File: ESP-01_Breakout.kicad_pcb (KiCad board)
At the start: 2 copper layers, 88.9 x 25.4 mm, 136 parts, among them J1 TBL003-254-02GR-2OR, SW1 SW_SPDT, U1 ESP-01v090, U2 R-78E5.0-0.5, U3 R-78E3.3-0.5

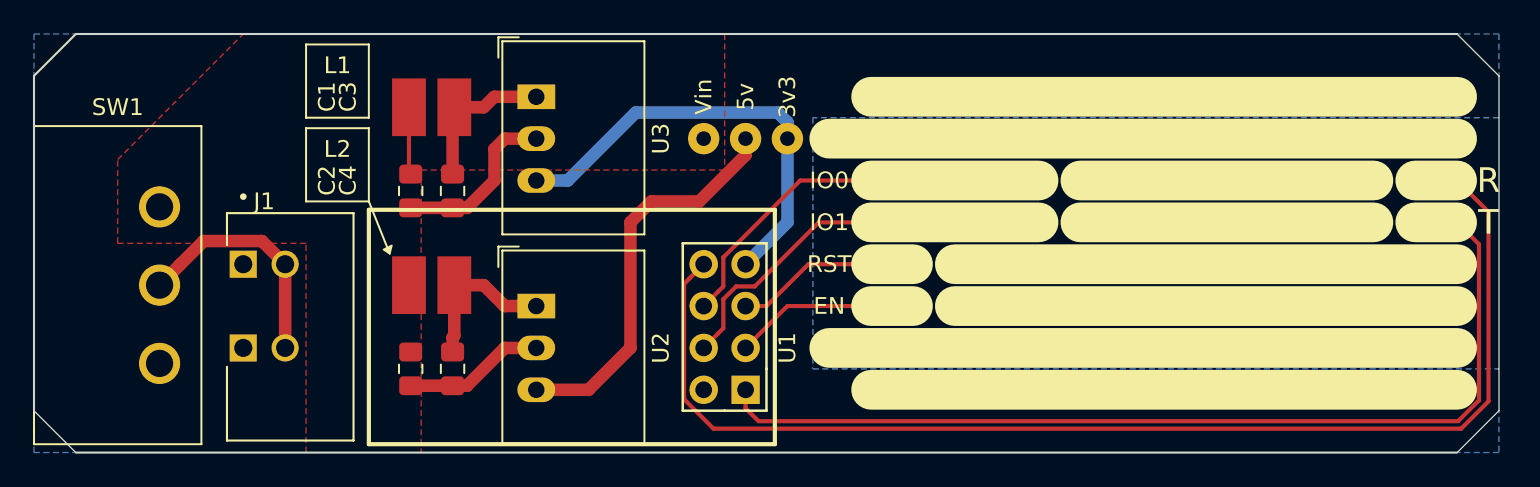
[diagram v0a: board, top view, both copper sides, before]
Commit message: Barrel Jack, Smaller Switch
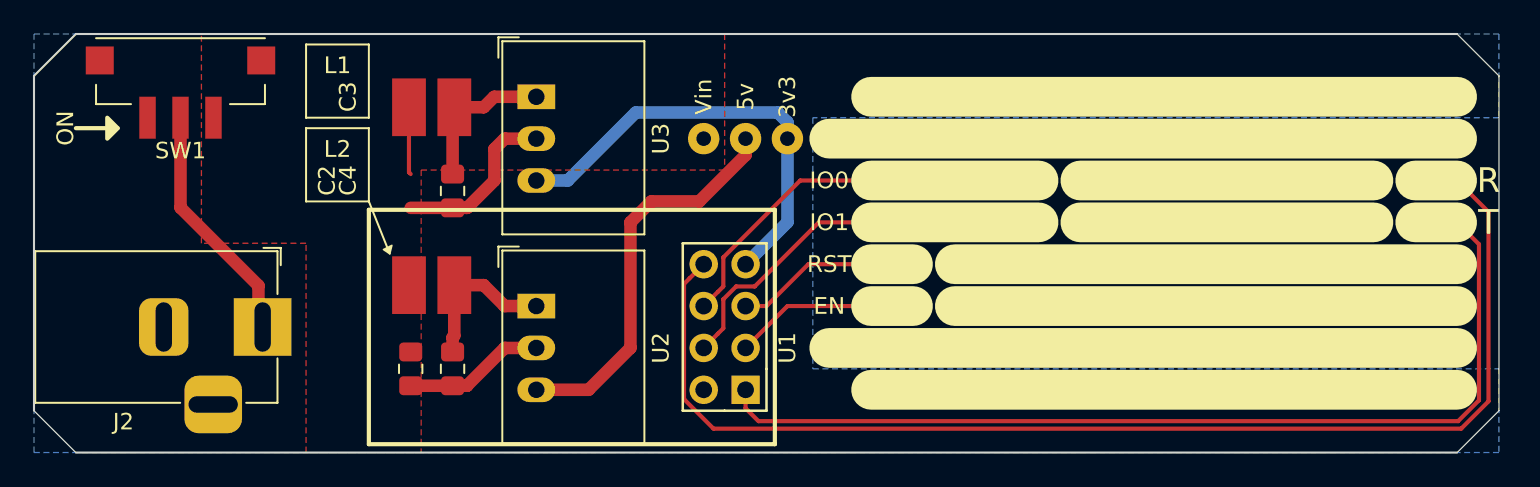
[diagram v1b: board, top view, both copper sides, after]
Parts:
- removed C1: 4.7uF, Capacitor_SMD:C_0805_2012Metric_Pad1.15x1.40mm_HandSolder
- removed J1: TBL003-254-02GR-2OR, TBL003-254-02GR-2OR:CUI_TBL003-254-02GR-2OR
- added J2: Barrel_Jack_Switch, ESP-01_Breakout:BarrelJack_Horizontal, F.Cu at (133.3, 95.2)
- added REF**: Symbol_Barrel_Polarity, Symbol:Symbol_Barrel_Polarity, B.Cu at (123.2, 95.3)
- SW1: footprint ESP-01_Breakout:L102011ML04Q -> ESP-01_Breakout:SS312SAH4-R
- moved SW1 10.2 mm to (128.3, 82.5)
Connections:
- SW1 pad 1: +12V -> /Off
- SW1 pad 3: /Off -> +12V
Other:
- board text added: "+"
- board text added: "-"
- board text added: "6-28v"
- board text added: "ON"
- board text removed: "- +"
- board text removed: "Vin: 6-28v"

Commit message: BOM, gitignore Update
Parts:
- added C1: 4.7uF, Capacitor_SMD:C_0805_2012Metric_Pad1.15x1.40mm_HandSolder, F.Cu at (142.2, 87.0)
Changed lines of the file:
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@@
     (tracks 87)
     (zones 0)
-    (modules 136)
+    (modules 137)
     (nets 22)
   )
   (page A4)
   (layers
-    (0 F.Cu signal hide)
-    (31 B.Cu signal)
+    (0 F.Cu signal)
+    (31 B.Cu signal hide)
     (32 B.Adhes user hide)
     (33 F.Adhes user hide)
-    (34 B.Paste user)
-    (35 F.Paste user hide)
-    (36 B.SilkS user)
-    (37 F.SilkS user hide)
-    (38 B.Mask user)
-    (39 F.Mask user hide)
+    (34 B.Paste user hide)
+    (35 F.Paste user)
+    (36 B.SilkS user hide)
+    (37 F.SilkS user)
+    (38 B.Mask user hide)
+    (39 F.Mask user)
     (40 Dwgs.User user hide)
     (41 Cmts.User user hide)
@@
     (44 Edge.Cuts user)
     (45 Margin user hide)
-    (46 B.CrtYd user)
-    (47 F.CrtYd user hide)
-    (48 B.Fab user)
-    (49 F.Fab user hide)
+    (46 B.CrtYd user hide)
+    (47 F.CrtYd user)
+    (48 B.Fab user hide)
+    (49 F.Fab user)
   )
   (setup
@@
       (usegerberattributes false)
       (usegerberadvancedattributes false)
-      (creategerberjobfile true)
+      (creategerberjobfile false)
       (excludeedgelayer true)
       (linewidth 0.127000)
@@
     (add_net "Net-(J2-Pad3)")
   )
+  (module Capacitor_SMD:C_0805_2012Metric_Pad1.15x1.40mm_HandSolder (layer F.Cu)
+    (at 142.24 86.995 270)
+    (descr "Capacitor SMD 0805 (2012 Metric), square (rectangular) end terminal, IPC_7351 nominal with elongated pad for handsoldering. (Body size source: https://docs.google.com/spreadsheets/d/1BsfQQcO9C6DZCsRaXUlFlo91Tg2WpOkGARC1WS5S8t0/edit?usp=sharing), generated with kicad-footprint-generator")
+    (tags "capacitor handsolder")
+    (attr smd)
+    (fp_text reference C1 (at -5.715 5.08 90) (layer F.SilkS)
+      (effects (font (size 1 1) (thickness 0.15)))
+    )
+    (fp_text value 4.7uF (at 0 1.65 90) (layer F.Fab)
+      (effects (font (size 1 1) (thickness 0.15)))
+    )
+    (fp_line (start 1.85 0.95) (end -1.85 0.95) (layer F.CrtYd) (width 0.05))
+    (fp_line (start 1.85 -0.95) (end 1.85 0.95) (layer F.CrtYd) (width 0.05))
+    (fp_line (start -1.85 -0.95) (end 1.85 -0.95) (layer F.CrtYd) (width 0.05))
+    (fp_line (start -1.85 0.95) (end -1.85 -0.95) (layer F.CrtYd) (width 0.05))
+    (fp_line (start -0.261252 0.71) (end 0.261252 0.71) (layer F.SilkS) (width 0.12))
+    (fp_line (start -0.261252 -0.71) (end 0.261252 -0.71) (layer F.SilkS) (width 0.12))
+    (fp_line (start 1 0.6) (end -1 0.6) (layer F.Fab) (width 0.1))
+    (fp_line (start 1 -0.6) (end 1 0.6) (layer F.Fab) (width 0.1))
+    (fp_line (start -1 -0.6) (end 1 -0.6) (layer F.Fab) (width 0.1))
+    (fp_line (start -1 0.6) (end -1 -0.6) (layer F.Fab) (width 0.1))
+    (pad 2 smd roundrect (at 1.025 0 270) (size 1.15 1.4) (layers F.Cu F.Paste F.Mask) (roundrect_rratio 0.217391)
+      (net 1 GND))
+    (pad 1 smd roundrect (at -1.025 0 270) (size 1.15 1.4) (layers F.Cu F.Paste F.Mask) (roundrect_rratio 0.217391)
+      (net 2 +12V))
+    (model ${KISYS3DMOD}/Capacitor_SMD.3dshapes/C_0805_2012Metric.wrl
+      (at (xyz 0 0 0))
+      (scale (xyz 1 1 1))
+      (rotate (xyz 0 0 0))
+    )
+  )
   (module Symbol:Symbol_Barrel_Polarity (layer B.Cu)

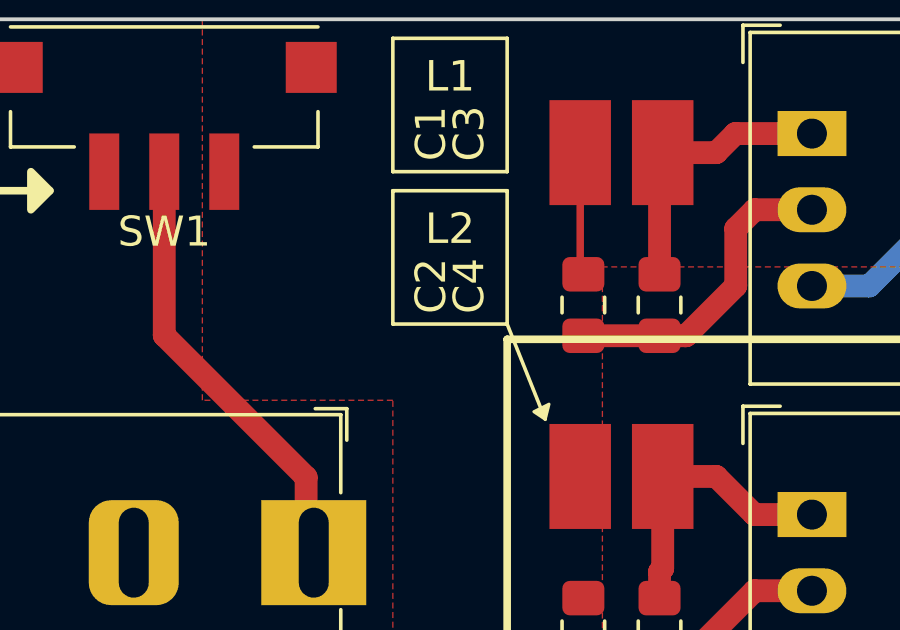
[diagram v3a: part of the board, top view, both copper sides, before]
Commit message: Add Inductor 3D Model
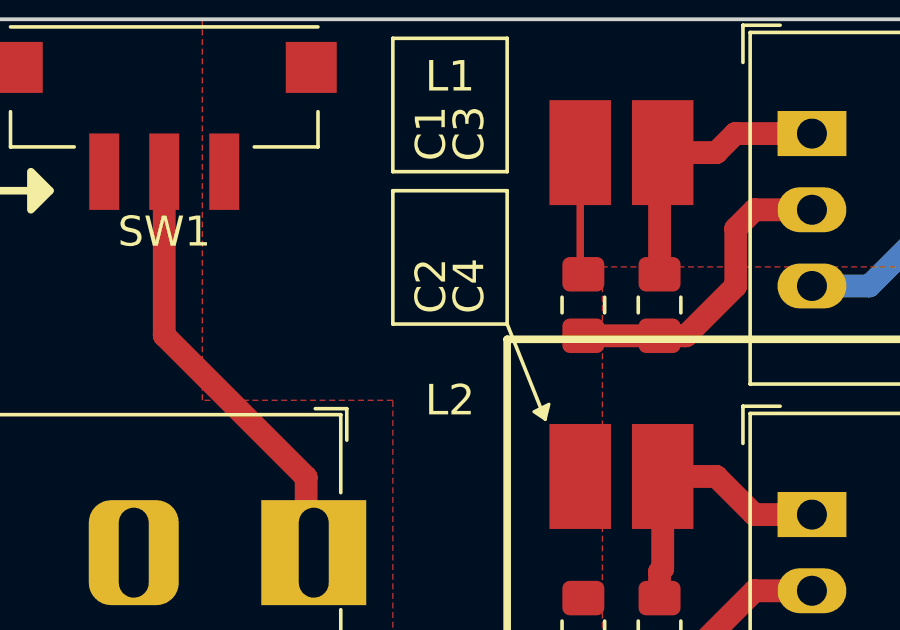
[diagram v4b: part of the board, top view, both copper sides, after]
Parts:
- L1, L2: footprint RLS-397:IND_RLS-397 -> ESP-01_Breakout:IND_RLS-397
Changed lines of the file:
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@@
     (solder_mask_min_width 0.25)
     (aux_axis_origin 0 0)
+    (grid_origin 119.38 102.87)
     (visible_elements FFFDFF7F)
     (pcbplotparams
@@
     (add_net "Net-(J2-Pad3)")
   )
+  (module ESP-01_Breakout:IND_RLS-397 (layer F.Cu)
+    (at 143.51 92.71)
+    (fp_text reference L2 (at -5.715 -2.54 180) (layer F.SilkS)
+      (effects (font (size 1.016 1.016) (thickness 0.1524)))
+    )
+    (fp_text value L (at 2.788 2.792) (layer F.Fab)
+      (effects (font (size 0.8 0.8) (thickness 0.015)))
+    )
+    (fp_line (start -2.25 -1.6) (end 2.25 -1.6) (layer F.Fab) (width 0.127))
+    (fp_line (start 2.25 -1.6) (end 2.25 1.6) (layer F.Fab) (width 0.127))
+    (fp_line (start 2.25 1.6) (end -2.25 1.6) (layer F.Fab) (width 0.127))
+    (fp_line (start -2.25 1.6) (end -2.25 -1.6) (layer F.Fab) (width 0.127))
+    (fp_line (start -2.66 -2.01) (end 2.66 -2.01) (layer F.CrtYd) (width 0.05))
+    (fp_line (start 2.66 -2.01) (end 2.66 2.01) (layer F.CrtYd) (width 0.05))
+    (fp_line (start 2.66 2.01) (end -2.66 2.01) (layer F.CrtYd) (width 0.05))
+    (fp_line (start -2.66 2.01) (end -2.66 -2.01) (layer F.CrtYd) (width 0.05))
+    (pad 1 smd rect (at -1.375 0) (size 2.05 3.5) (layers F.Cu F.Paste F.Mask)
+      (net 2 +12V))
+    (pad 2 smd rect (at 1.375 0) (size 2.05 3.5) (layers F.Cu F.Paste F.Mask)
+      (net 4 "Net-(C4-Pad1)"))
+    (model ${KIPRJMOD}/3D_Files/RLS-126-R--3DModel-STEP-1.STEP
+      (at (xyz 0 0 0))
+      (scale (xyz 1 1 1))
+      (rotate (xyz -90 0 0))
+    )
+  )
+  (module ESP-01_Breakout:IND_RLS-397 (layer F.Cu)
+    (at 143.51 81.915)
+    (fp_text reference L1 (at -5.715 -2.54 180) (layer F.SilkS)
+      (effects (font (size 1.016 1.016) (thickness 0.1524)))
+    )
+    (fp_text value L (at 2.788 2.792) (layer F.Fab)
+      (effects (font (size 0.8 0.8) (thickness 0.015)))
+    )
+    (fp_line (start -2.25 -1.6) (end 2.25 -1.6) (layer F.Fab) (width 0.127))
+    (fp_line (start 2.25 -1.6) (end 2.25 1.6) (layer F.Fab) (width 0.127))
+    (fp_line (start 2.25 1.6) (end -2.25 1.6) (layer F.Fab) (width 0.127))
+    (fp_line (start -2.25 1.6) (end -2.25 -1.6) (layer F.Fab) (width 0.127))
+    (fp_line (start -2.66 -2.01) (end 2.66 -2.01) (layer F.CrtYd) (width 0.05))
+    (fp_line (start 2.66 -2.01) (end 2.66 2.01) (layer F.CrtYd) (width 0.05))
+    (fp_line (start 2.66 2.01) (end -2.66 2.01) (layer F.CrtYd) (width 0.05))
+    (fp_line (start -2.66 2.01) (end -2.66 -2.01) (layer F.CrtYd) (width 0.05))
+    (pad 1 smd rect (at -1.375 0) (size 2.05 3.5) (layers F.Cu F.Paste F.Mask)
+      (net 2 +12V))
+    (pad 2 smd rect (at 1.375 0) (size 2.05 3.5) (layers F.Cu F.Paste F.Mask)
+      (net 3 "Net-(C3-Pad1)"))
+    (model ${KIPRJMOD}/3D_Files/RLS-126-R--3DModel-STEP-1.STEP
+      (at (xyz 0 0 0))
+      (scale (xyz 1 1 1))
+      (rotate (xyz -90 0 0))
+    )
+  )
   (module ESP-01_Breakout:SS312SAH4-R (layer F.Cu)
     (at 128.27 82.55 270)
@@
     (fp_text value 4.7uF (at 0 1.65 90) (layer F.Fab)
       (effects (font (size 1 1) (thickness 0.15)))
+    )
+    (fp_text user %R (at 0 0 90) (layer F.Fab)
+      (effects (font (size 0.5 0.5) (thickness 0.08)))
     )
     (fp_line (start 1.85 0.95) (end -1.85 0.95) (layer F.CrtYd) (width 0.05))
@@
       (rotate (xyz -90 0 90))
     )
-  )
-  (module RLS-397:IND_RLS-397 (layer F.Cu)
-    (at 143.51 81.915)
-    (fp_text reference L1 (at -5.715 -2.54 180) (layer F.SilkS)
-      (effects (font (size 1.016 1.016) (thickness 0.1524)))
-    )
-    (fp_text value L (at 2.788 2.792) (layer F.Fab)
-      (effects (font (size 0.8 0.8) (thickness 0.015)))
-    )
-    (fp_line (start -2.66 2.01) (end -2.66 -2.01) (layer F.CrtYd) (width 0.05))
-    (fp_line (start 2.66 2.01) (end -2.66 2.01) (layer F.CrtYd) (width 0.05))
-    (fp_line (start 2.66 -2.01) (end 2.66 2.01) (layer F.CrtYd) (width 0.05))
-    (fp_line (start -2.66 -2.01) (end 2.66 -2.01) (layer F.CrtYd) (width 0.05))
-    (fp_line (start -2.25 1.6) (end -2.25 -1.6) (layer F.Fab) (width 0.127))
-    (fp_line (start 2.25 1.6) (end -2.25 1.6) (layer F.Fab) (width 0.127))
-    (fp_line (start 2.25 -1.6) (end 2.25 1.6) (layer F.Fab) (width 0.127))
-    (fp_line (start -2.25 -1.6) (end 2.25 -1.6) (layer F.Fab) (width 0.127))
-    (pad 2 smd rect (at 1.375 0) (size 2.05 3.5) (layers F.Cu F.Paste F.Mask)
-      (net 3 "Net-(C3-Pad1)"))
-    (pad 1 smd rect (at -1.375 0) (size 2.05 3.5) (layers F.Cu F.Paste F.Mask)
-      (net 2 +12V))
   )
   (module ESP-01_Breakout:TP (layer F.Cu)
@@
     )
   )
-  (module RLS-397:IND_RLS-397 (layer F.Cu)
-    (at 143.51 92.71)
-    (fp_text reference L2 (at -5.715 -8.255) (layer F.SilkS)
-      (effects (font (size 1.016 1.016) (thickness 0.1524)))
-    )
-    (fp_text value L (at 2.788 2.792) (layer F.Fab)
-      (effects (font (size 0.8 0.8) (thickness 0.015)))
-    )
-    (fp_line (start -2.66 2.01) (end -2.66 -2.01) (layer F.CrtYd) (width 0.05))
-    (fp_line (start 2.66 2.01) (end -2.66 2.01) (layer F.CrtYd) (width 0.05))
-    (fp_line (start 2.66 -2.01) (end 2.66 2.01) (layer F.CrtYd) (width 0.05))
-    (fp_line (start -2.66 -2.01) (end 2.66 -2.01) (layer F.CrtYd) (width 0.05))
-    (fp_line (start -2.25 1.6) (end -2.25 -1.6) (layer F.Fab) (width 0.127))
-    (fp_line (start 2.25 1.6) (end -2.25 1.6) (layer F.Fab) (width 0.127))
-    (fp_line (start 2.25 -1.6) (end 2.25 1.6) (layer F.Fab) (width 0.127))
-    (fp_line (start -2.25 -1.6) (end 2.25 -1.6) (layer F.Fab) (width 0.127))
-    (pad 2 smd rect (at 1.375 0) (size 2.05 3.5) (layers F.Cu F.Paste F.Mask)
-      (net 4 "Net-(C4-Pad1)"))
-    (pad 1 smd rect (at -1.375 0) (size 2.05 3.5) (layers F.Cu F.Paste F.Mask)
-      (net 2 +12V))
-  )
   (module Capacitor_SMD:C_0805_2012Metric_Pad1.15x1.40mm_HandSolder (layer F.Cu)

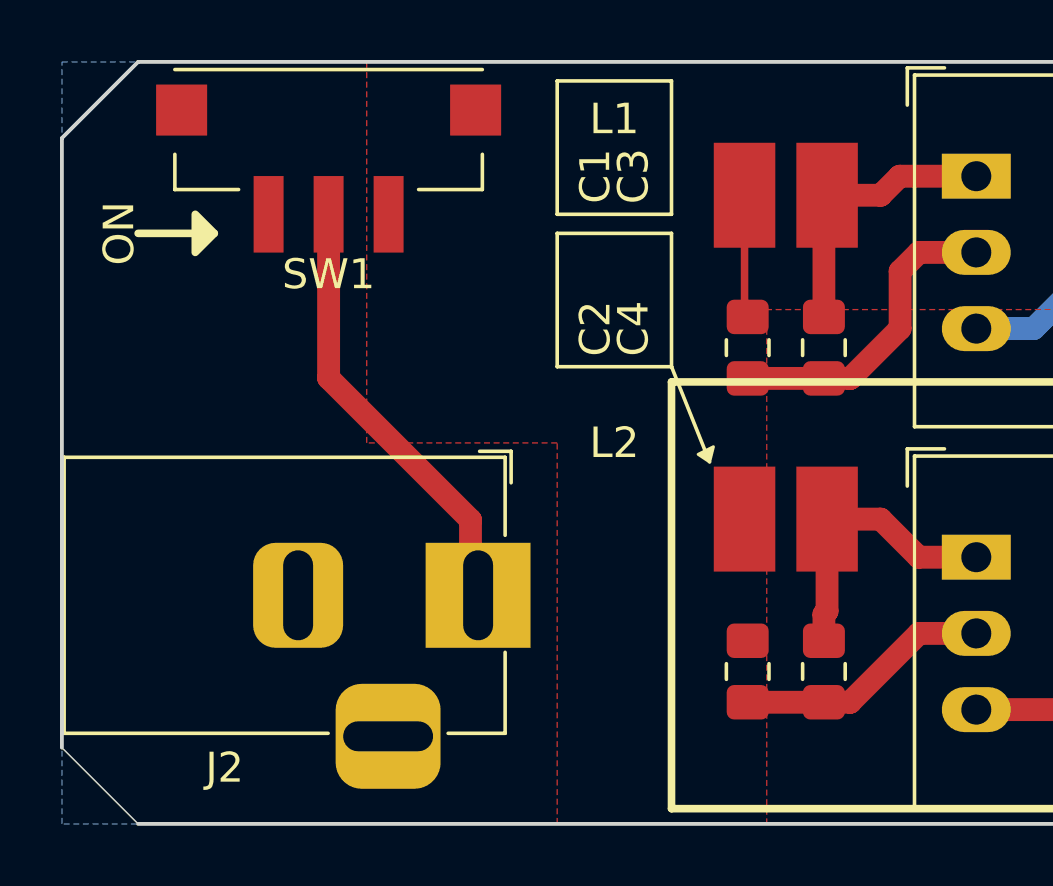
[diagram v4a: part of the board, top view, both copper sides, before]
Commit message: Updated Footprints, Added 5v Solder Jumper
Slight tweak to silkscreen tezt
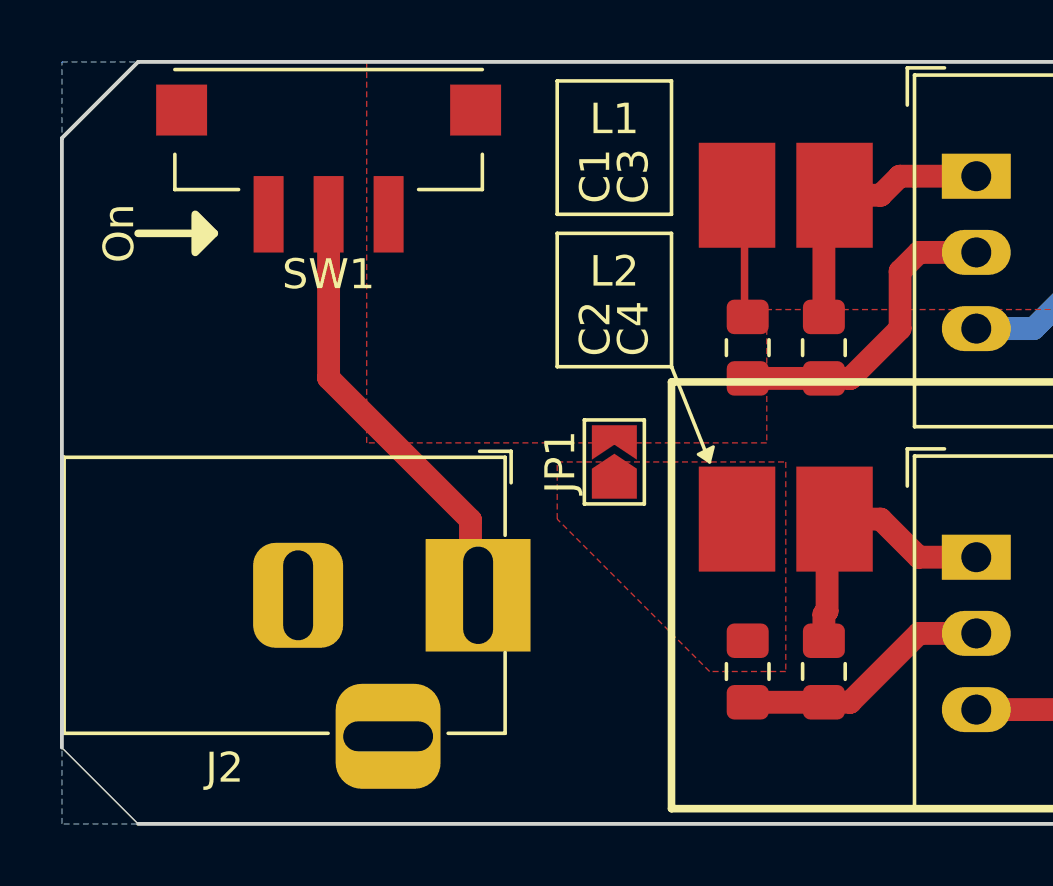
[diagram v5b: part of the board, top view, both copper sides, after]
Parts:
- added JP1: SolderJumper_2_Open, Jumper:SolderJumper-2_P1.3mm_Open_TrianglePad1.0x1.5mm, F.Cu at (137.8, 90.8)
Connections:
- C2 pad 1: +12V -> Net-(C2-Pad1)
- L2 pad 1: +12V -> Net-(C2-Pad1)
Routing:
- added copper zone on F.Cu, net Net-(C2-Pad1)
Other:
- board text added: "On"
- board text removed: "ON"
